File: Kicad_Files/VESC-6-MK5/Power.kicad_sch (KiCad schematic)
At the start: 49 parts, among them P10 PH_C, P11 SUPPLY, P12 GND, P8 PH_A, P9 PH_B, Q1 IRF7749, Q2 IRF7749, Q3 IRF7749, Q4 IRF7749, Q5 IRF7749, Q6 IRF7749, U10 MC74VHC1GT66, U12 MC74VHC1GT66, U13 MC74VHC1GT66, U5 AD8418, U6 AD8418, U7 AD8418

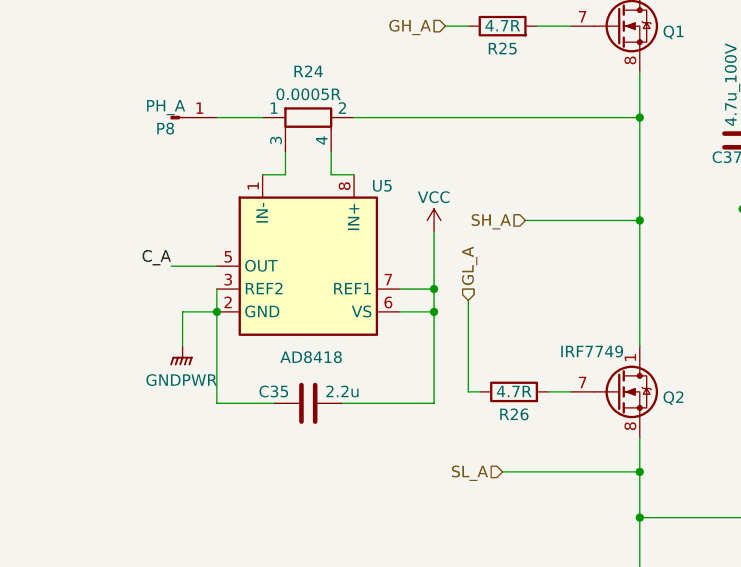
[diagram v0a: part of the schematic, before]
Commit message: Moved current sense amplifiers next to the shunt resistors
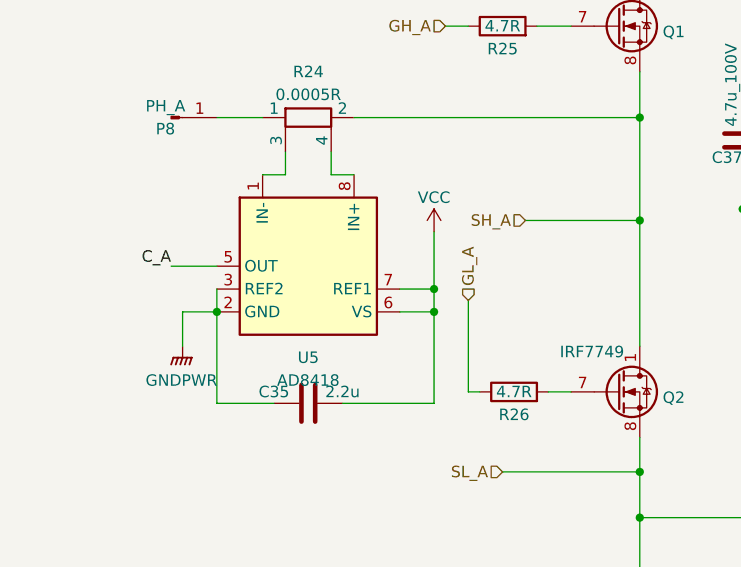
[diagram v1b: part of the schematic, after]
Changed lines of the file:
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@@
   (symbol (lib_name "AD8418_1") (lib_id "Amplifier_Current:AD8418") (at 45.72 68.58 0) (unit 1)
     (in_bom yes) (on_board yes) (dnp no) (fields_autoplaced)
-    (property "Reference" "U5" (at 52.7559 59.69 0)
-      (effects (font (size 1.27 1.27)) (justify left))
+    (property "Reference" "U5" (at 45.72 78.74 0)
+      (effects (font (size 1.27 1.27)))
     )
-    (property "Value" "AD8418" (at 42.5959 78.74 0)
-      (effects (font (size 1.27 1.27)) (justify left))
+    (property "Value" "AD8418" (at 45.72 81.28 0)
+      (effects (font (size 1.27 1.27)))
     )
     (property "Footprint" "Power_:SOP65P490X110-8N" (at 41.91 74.93 0)

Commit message: Working sample of the display
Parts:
- R27: footprint DRV8301_:RESC1608X55N -> DRV8301_:THERM_ERT-JZEG103FA
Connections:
- net GNDPWR is gone; now on net GND: C29.2, C30.2, C35.1, C37.1, C38.1, C39.1, C40.1, C41.1, C42.1, C43.1, C44.1, C45.2, C46.2, C47.2, C52.2, C53.2, C54.2, P12.1 (Pin_1), Q2.8 (S), Q4.8 (S), Q6.8 (S), U10.3 (GND), U12.3 (GND), U13.3 (GND), U5.2 (GND), U5.3 (REF2), U6.2 (GND), U6.3 (REF2), U7.2 (GND), U7.3 (REF2)
